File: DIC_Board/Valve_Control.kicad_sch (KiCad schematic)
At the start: 10 parts, among them U20 DRV8823QDCARQ1

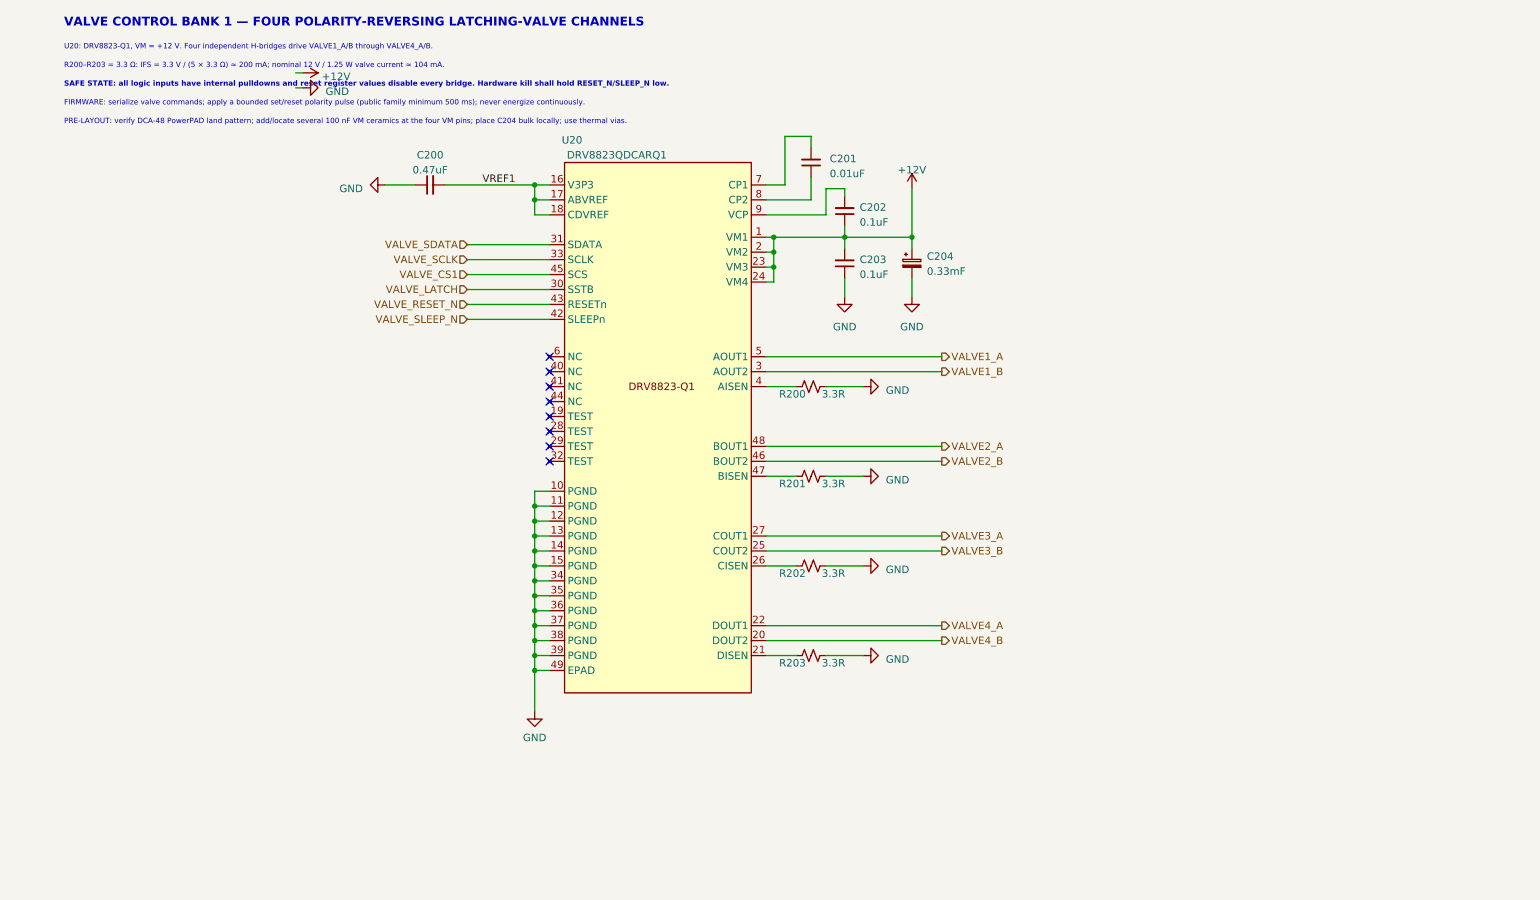
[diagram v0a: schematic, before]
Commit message: added valve control banks.
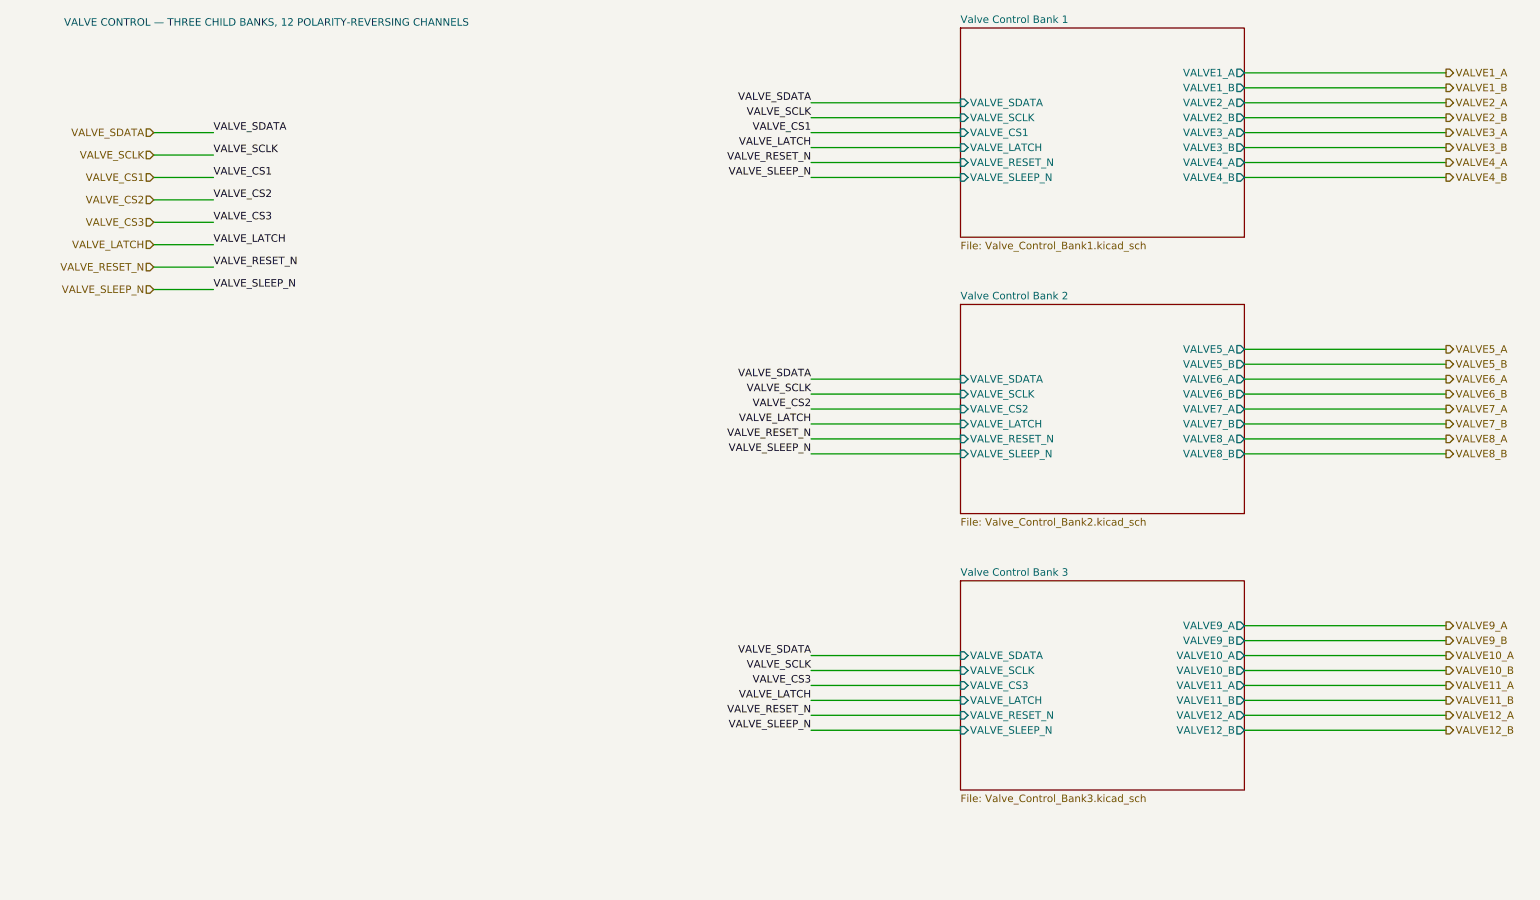
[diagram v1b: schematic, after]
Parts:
- removed C200: 0.47uF, Capacitor_SMD:C_0603_1608Metric_Pad1.08x0.95mm_HandSolder, symbol Device:C_Small
- removed C201: 0.01uF, Capacitor_SMD:C_0603_1608Metric_Pad1.08x0.95mm_HandSolder, symbol Device:C_Small
- removed C202, C203: 0.1uF, Capacitor_SMD:C_0603_1608Metric_Pad1.08x0.95mm_HandSolder, symbol Device:C_Small
- removed C204: 0.33mF, Capacitor_THT:CP_Radial_D12.5mm_P5.00mm, symbol Device:C_Polarized_Small
- removed R200, R201, R202, R203: 3.3R, Resistor_SMD:R_1206_3216Metric, symbol Device:R_Small_US
- removed U20: DRV8823QDCARQ1, DIC_Board:HTSSOP48, symbol DIC_Board:DRV8823QDCARQ1
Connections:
- no-connect marks 8 -> 0
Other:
- added sheet Valve Control Bank 1 (Valve_Control_Bank1.kicad_sch)
- added sheet Valve Control Bank 2 (Valve_Control_Bank2.kicad_sch)
- added sheet Valve Control Bank 3 (Valve_Control_Bank3.kicad_sch)
- note added: "VALVE CONTROL — THREE CHILD BANKS, 12 POLARITY-REVERSING CHANNELS"
- note removed: "FIRMWARE: serialize valve commands; apply a bounded set/reset polarity pulse (public family minimum 500 ms); never energize continuously."
- note removed: "PRE-LAYOUT: verify DCA-48 PowerPAD land pattern; add/locate several 100 nF VM ceramics at the four VM pins; place C204 bulk locally; use thermal vias."
- note removed: "R200–R203 = 3.3 Ω: IFS = 3.3 V / (5 × 3.3 Ω) ≈ 200 mA; nominal 12 V / 1.25 W valve current ≈ 104 mA."
- note removed: "SAFE STATE: all logic inputs have internal pulldowns and reset register values disable every bridge. Hardware kill shall hold RESET_N/SLEEP_N low."
- note removed: "U20: DRV8823-Q1, VM = +12 V. Four independent H-bridges drive VALVE1_A/B through VALVE4_A/B."
- note removed: "VALVE CONTROL BANK 1 — FOUR POLARITY-REVERSING LATCHING-VALVE CHANNELS"
- title: Valve Control Bank 1 -> Valve Control

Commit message: Added Sheets for pumps and sensors
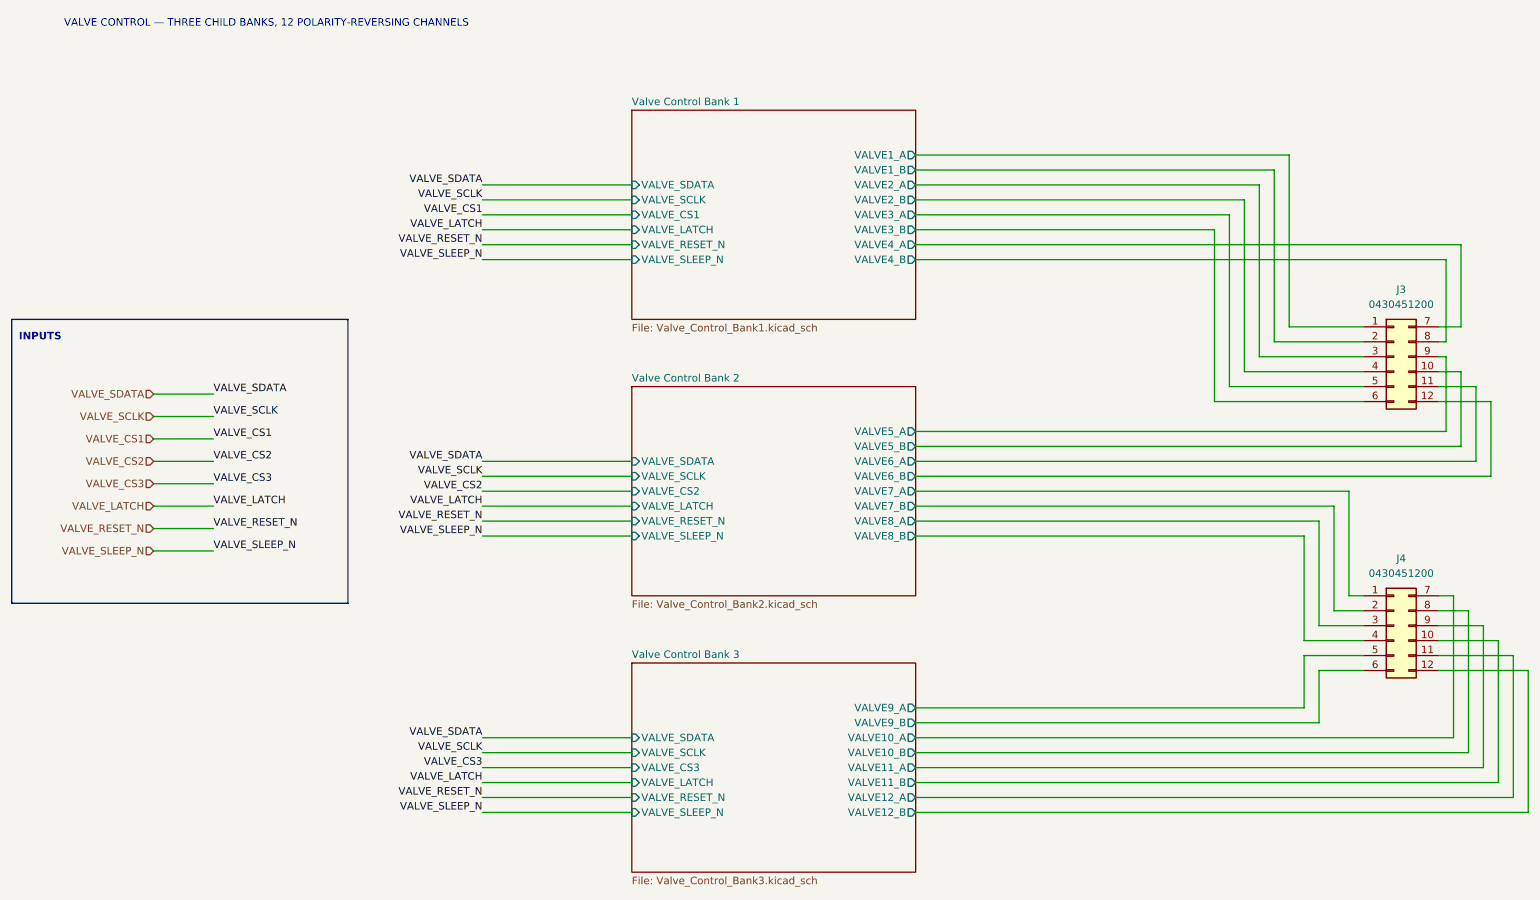
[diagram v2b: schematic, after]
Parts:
- added J3, J4: 0430451200, DIC_Board:Molex_Micro-Fit_3.0_43045-1200_2x06_P3.00mm_Horizontal, symbol DIC_Board:Molex_0430451200
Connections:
- new net Valve Control Bank 1/VALVE1_A: J3.1 (Pin_1)
- new net Valve Control Bank 1/VALVE1_B: J3.2 (Pin_2)
- new net Valve Control Bank 1/VALVE2_A: J3.3 (Pin_3)
- new net Valve Control Bank 1/VALVE2_B: J3.4 (Pin_4)
- new net Valve Control Bank 1/VALVE3_A: J3.5 (Pin_5)
- new net Valve Control Bank 1/VALVE3_B: J3.6 (Pin_6)
- new net Valve Control Bank 1/VALVE4_A: J3.7 (Pin_7)
- new net Valve Control Bank 1/VALVE4_B: J3.8 (Pin_8)
- new net Valve Control Bank 2/VALVE5_A: J3.9 (Pin_9)
- new net Valve Control Bank 2/VALVE5_B: J3.10 (Pin_10)
- new net Valve Control Bank 2/VALVE6_A: J3.11 (Pin_11)
- new net Valve Control Bank 2/VALVE6_B: J3.12 (Pin_12)
- new net Valve Control Bank 2/VALVE7_A: J4.1 (Pin_1)
- new net Valve Control Bank 2/VALVE7_B: J4.2 (Pin_2)
- new net Valve Control Bank 2/VALVE8_A: J4.3 (Pin_3)
- new net Valve Control Bank 2/VALVE8_B: J4.4 (Pin_4)
- new net Valve Control Bank 3/VALVE10_A: J4.7 (Pin_7)
- new net Valve Control Bank 3/VALVE10_B: J4.8 (Pin_8)
- new net Valve Control Bank 3/VALVE11_A: J4.9 (Pin_9)
- new net Valve Control Bank 3/VALVE11_B: J4.10 (Pin_10)
- new net Valve Control Bank 3/VALVE12_A: J4.11 (Pin_11)
- new net Valve Control Bank 3/VALVE12_B: J4.12 (Pin_12)
- new net Valve Control Bank 3/VALVE9_A: J4.5 (Pin_5)
- new net Valve Control Bank 3/VALVE9_B: J4.6 (Pin_6)
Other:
- note added: "INPUTS"

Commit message: Updated board for layout! All footprints added
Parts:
- J3, J4: Design Confirmation (none) -> 2026-09-11: User accepted the existing nominal 12V supply f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
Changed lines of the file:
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@@
+			)
+		)
+		(property "Design Confirmation" "2026-09-11: User accepted the existing nominal 12V supply for the valves. Exact pulse/current and firmware qualification are separate."
+			(at 0 0 0)
+			(hide yes)
+			(show_name no)
+			(do_not_autoplace no)
+			(effects
+				(font
+					(size 1.27 1.27)
+				)
 			)
 		)
@@
 			(hide yes)
 			(show_name no)
+			(do_not_autoplace no)
+			(effects
+				(font
+					(size 1.27 1.27)
+				)
+			)
+		)
+		(property "Design Confirmation" "2026-09-11: User accepted the existing nominal 12V supply for the valves. Exact pulse/current and firmware qualification are separate."
+			(at 0 0 0)
+			(hide yes)
+			(show_name no)
